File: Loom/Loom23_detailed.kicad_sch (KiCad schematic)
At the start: 7 parts

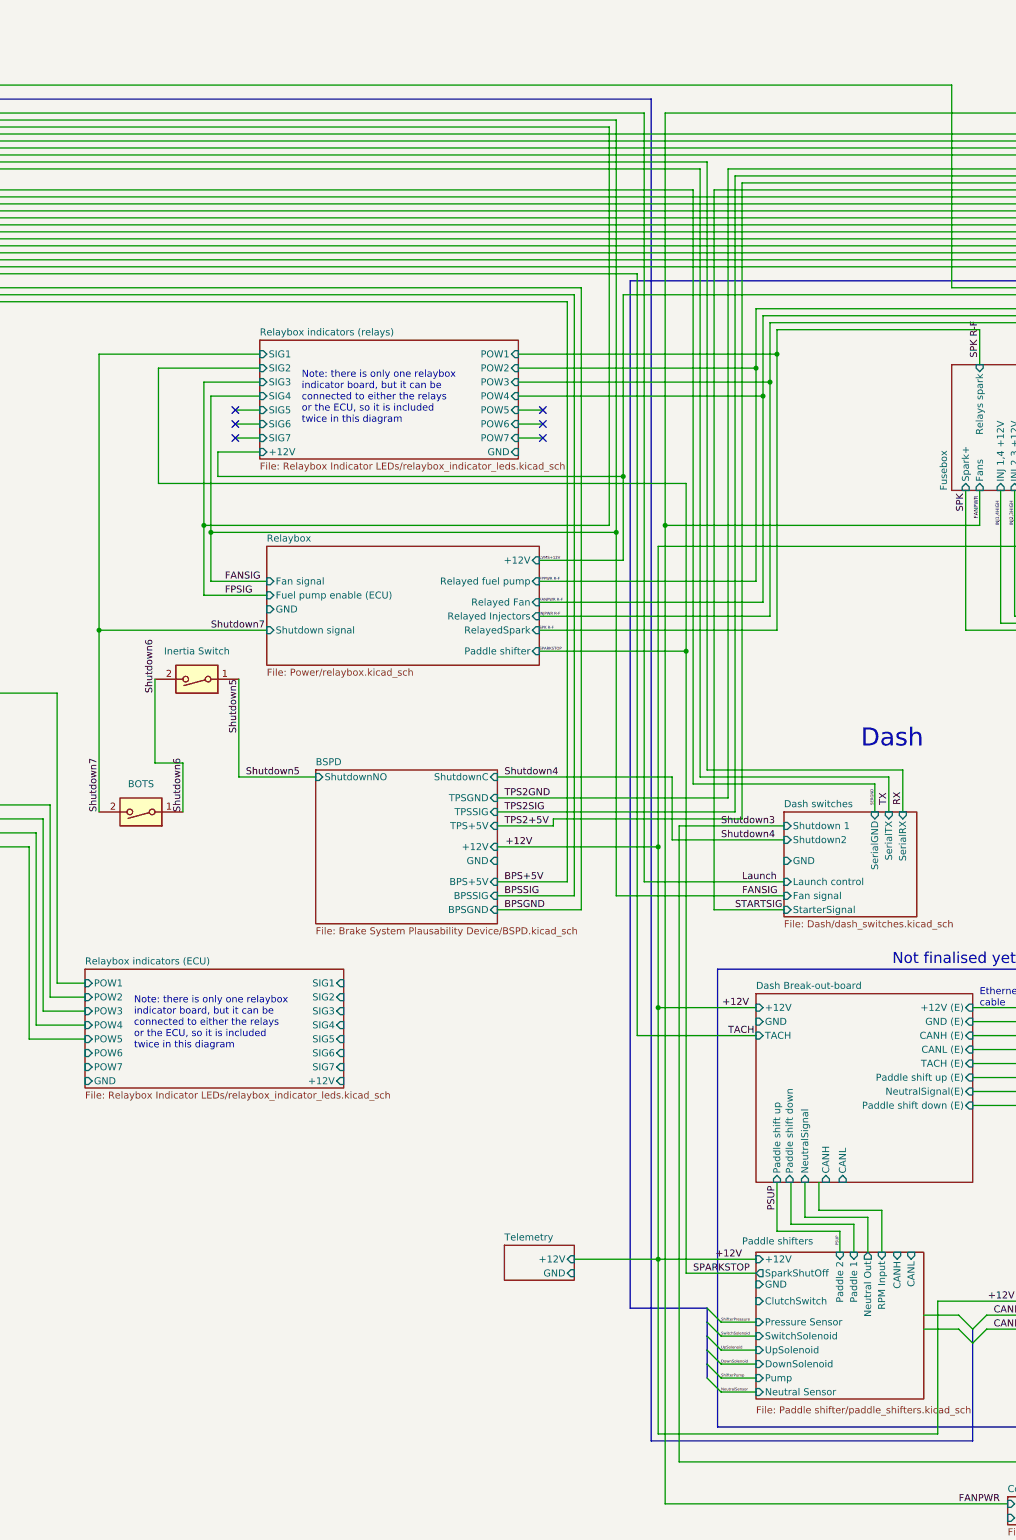
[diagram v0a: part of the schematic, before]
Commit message: Added the neutral and shutdown LEDs to dash
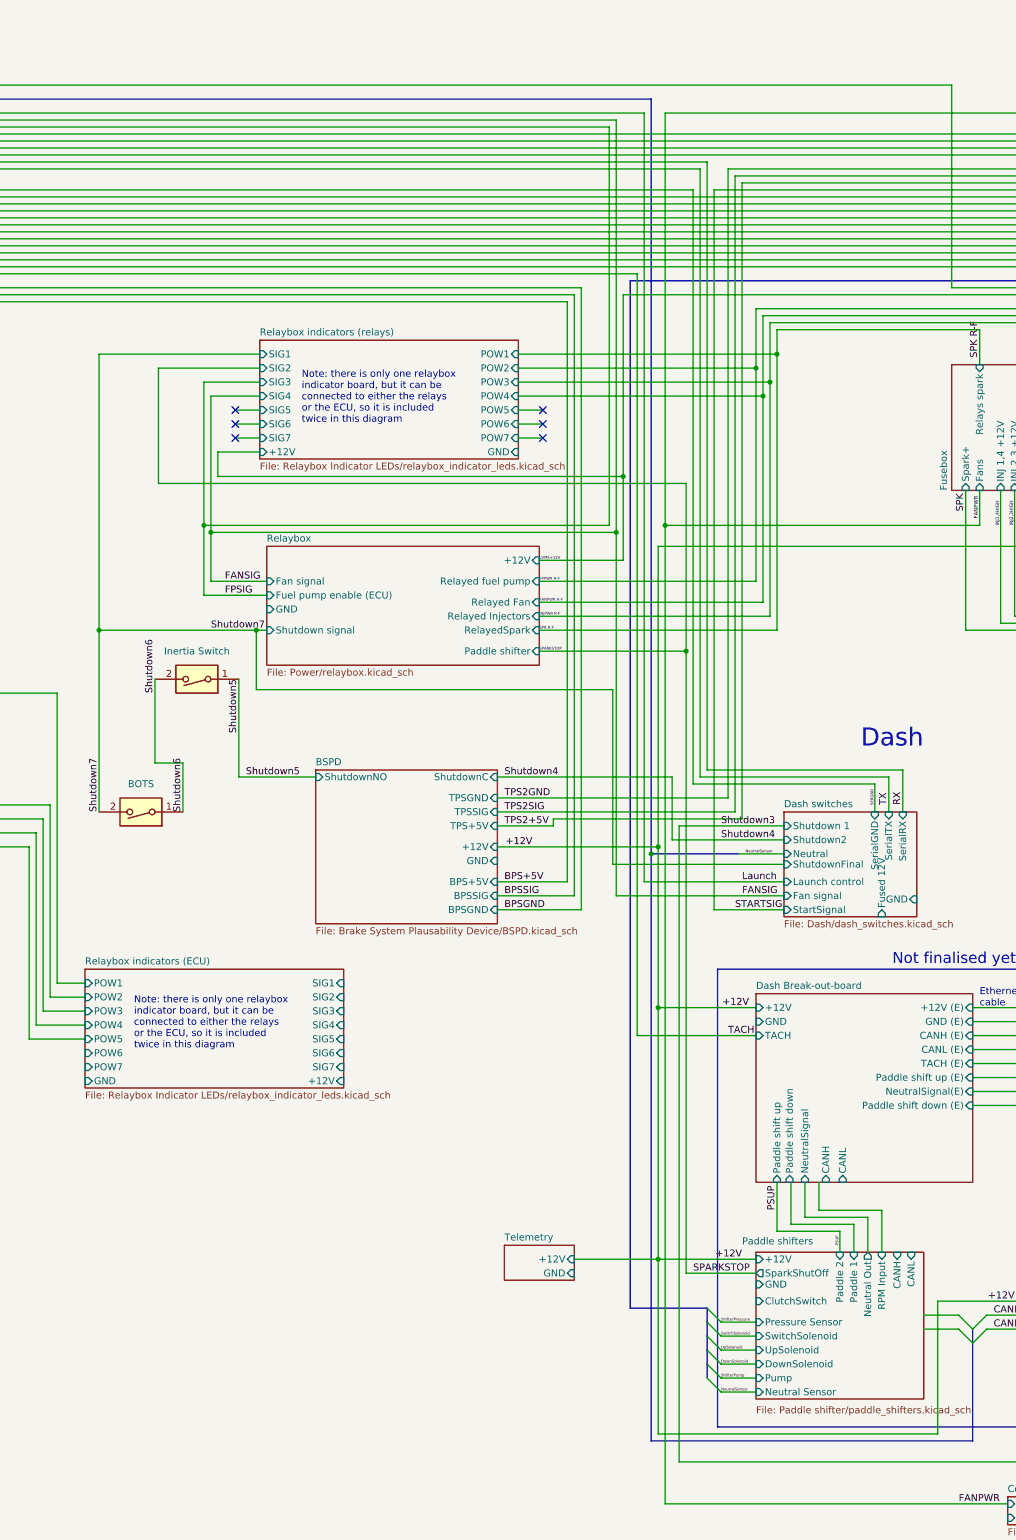
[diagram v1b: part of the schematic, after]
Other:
- sheet Dash switches ports: added Fused 12V, Neutral, ShutdownFinal, StartSignal; removed StarterSignal
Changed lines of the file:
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@@
   (junction (at 375.92 102.87) (diameter 0) (color 0 0 0 0)
   )
+  (junction (at 232.41 189.23) (diameter 0) (color 0 0 0 0)
+  )
   (junction (at 226.06 130.81) (diameter 0) (color 0 0 0 0)
   )
@@
   )
   (junction (at 384.81 228.6) (diameter 0) (color 0 0 0 0)
+  )
+  (junction (at 160.655 148.59) (diameter 0) (color 0 0 0 0)
   )
   (junction (at 83.82 203.2) (diameter 0) (color 0 0 0 0)
@@
     (stroke (width 0) (type default) (color 194 194 194 1))
   )
+  (wire (pts (xy 225.425 159.385) (xy 225.425 191.135))
+    (stroke (width 0) (type default))
+  )
   (wire (pts (xy 353.06 165.1) (xy 384.81 165.1))
     (stroke (width 0) (type default) (color 0 0 255 1))
@@
     (stroke (width 0) (type default) (color 0 255 0 1))
   )
+  (wire (pts (xy 160.655 148.59) (xy 160.655 159.385))
+    (stroke (width 0) (type default))
+  )
   (wire (pts (xy 384.81 228.6) (xy 415.29 228.6))
     (stroke (width 0) (type default) (color 0 0 255 1))
@@
     (stroke (width 0) (type default))
   )
+  (wire (pts (xy 248.285 189.23) (xy 256.54 189.23))
+    (stroke (width 0) (type default))
+  )
   (polyline (pts (xy 467.36 73.66) (xy 476.25 73.66))
     (stroke (width 0) (type default))
@@
     (stroke (width 0) (type default))
   )
-  (bus (pts (xy 232.41 52.07) (xy 232.41 295.91))
+  (bus (pts (xy 232.41 52.07) (xy 232.41 189.23))
     (stroke (width 0) (type default))
   )
@@
     (stroke (width 0) (type default))
   )
+  (wire (pts (xy 160.655 148.59) (xy 132.08 148.59))
+    (stroke (width 0) (type default))
+  )
   (wire (pts (xy 90.17 226.06) (xy 90.17 76.2))
     (stroke (width 0) (type default) (color 0 255 0 1))
@@
     (stroke (width 0) (type default))
   )
+  (bus (pts (xy 232.41 189.23) (xy 248.285 189.23))
+    (stroke (width 0) (type default))
+  )
   (wire (pts (xy 327.66 31.75) (xy 318.77 31.75))
     (stroke (width 0) (type default))
@@
   )
   (wire (pts (xy 62.23 195.58) (xy 68.58 195.58))
+    (stroke (width 0) (type default))
+  )
+  (wire (pts (xy 225.425 191.135) (xy 256.54 191.135))
     (stroke (width 0) (type default))
   )
@@
     (stroke (width 0) (type default))
   )
-  (wire (pts (xy 162.56 148.59) (xy 132.08 148.59))
+  (wire (pts (xy 162.56 148.59) (xy 160.655 148.59))
     (stroke (width 0) (type default))
   )
@@
     (stroke (width 0) (type default) (color 0 255 0 1))
   )
+  (wire (pts (xy 160.655 159.385) (xy 225.425 159.385))
+    (stroke (width 0) (type default))
+  )
   (wire (pts (xy 355.6 78.74) (xy 355.6 176.53))
     (stroke (width 0) (type default) (color 0 255 0 1))
@@
     (stroke (width 0) (type default) (color 0 0 255 1))
   )
+  (bus (pts (xy 232.41 189.23) (xy 232.41 295.91))
+    (stroke (width 0) (type default))
+  )
   (wire (pts (xy 142.875 100.965) (xy 142.875 121.92))
     (stroke (width 0) (type default))
@@
   (label "SENGND" (at 384.81 97.79 180) (fields_autoplaced)
     (effects (font (size 0.4 0.4)) (justify right bottom))
+  )
+  (label "NeutralSensor" (at 249.555 189.23 0) (fields_autoplaced)
+    (effects (font (size 0.5 0.5)) (justify left bottom))
   )
   (label "BPSSIG" (at 205.74 196.85 0) (fields_autoplaced)
@@
       (effects (font (size 1.27 1.27)) (justify left top))
     )
-    (pin "GND" input (at 256.54 190.5 180)
-      (effects (font (size 1.27 1.27)) (justify left))
+    (pin "GND" input (at 280.67 197.485 0)
+      (effects (font (size 1.27 1.27)) (justify right))
     )
     (pin "Shutdown 1" input (at 256.54 184.15 180)
@@
       (effects (font (size 1.27 1.27)) (justify left))
     )
-    (pin "StarterSignal" input (at 256.54 199.39 180)
-      (effects (font (size 1.27 1.27)) (justify left))
-    )
     (pin "Fan signal" input (at 256.54 196.85 180)
       (effects (font (size 1.27 1.27)) (justify left))
@@
       (effects (font (size 1.27 1.27)) (justify right))
     )
+    (pin "Fused 12V" input (at 274.32 200.66 270)
+      (effects (font (size 1.27 1.27)) (justify left))
+    )
+    (pin "ShutdownFinal" input (at 256.54 191.135 180)
+      (effects (font (size 1.27 1.27)) (justify left))
+    )
+    (pin "StartSignal" input (at 256.54 199.39 180)
+      (effects (font (size 1.27 1.27)) (justify left))
+    )
+    (pin "Neutral" input (at 256.54 189.23 180)
+      (effects (font (size 1.27 1.27)) (justify left))
+    )
     (instances
